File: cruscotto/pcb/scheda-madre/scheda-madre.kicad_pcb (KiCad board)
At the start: 4 copper layers, 178.7 x 74 mm, 148 parts, among them J1 Micro-Fit 2x12 verso auto (D-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, J10 Verso P1 S3: 5V TXD RXD GND, J11 Verso P2 S3: IO19 IO11 IO12 I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, J12 Verso P6 Speak S3, J3 USB-C (solo a banco), J4 Ventola Delta AFB0412VA-00 (D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, J5 NTC display, J6 STEVAL-MKI196V1 (DIL-24), J7 Modulo MicroSD: 3V3 CS MOSI C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, J8 Modulo VAN: 3.3V GND RX TX, J9 Modulo VAN: CANH CANL, K1 G2RL-2 DC5, K2 G2RL-2 DC5, Q1 IPD50N06S4L-12 (da confermare), Q3 ZXMP6A13F (P 60 V), Q4 MMBTA06 (80 V), Q5 MMBT3904, Q6 MMBT3904, Q7 MMBT3904, Q8 MMBT5551, Q9 AO3400A, SW3 RESET, SW4 BOOT, U1 LM74700-Q1, U10 DS3231SN, U2 TPS54360B, U3 LMR36510, U4 ESP32-WROOM-32E-H4, U5 AP2112K-3.3, U6 CH340C, U7 LM2903B, U9 AP2112K-3.3

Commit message: feat(bom): power parts verified (Q1, L1, L2, C3), complete purchase list per supplier
- Verification 28/10/2026 from DigiKey parameters and TI pages: IPD50N06S4L-12 (0.06 W at 2.2 A,
  LM74700 gate 12.1-13 V below VGS 16 V), SRR1260-8R2Y (Isat 5.8 A, peak 2.45 A at 2 A load),
  SRN6045TA-220M (Isat 3.3 A, peak 1.17 A), EEU-FR1H221 (about 1 ms ride-through; 17.5 mm tall:
  mount lying down). Schematic EL-001 rev D values and notes, board values updated; DRC unchanged
  (0 errors, 0 unconnected).
- lista-acquisti-scheda-madre.md: LCSC cart (55 lines, 84.52 USD + 13 USD shipping), Farnell quick
  order (16 lines incl. second STEVAL and Micro-Fit bench plug), DigiKey L1 and fan, second MicroSD
  and VAN modules, PCB after Gerbers.

Co-Authored-By: Claude Opus 5.5 <noreply@anthropic.com>
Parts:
- L1: value 8.2uH Isat>=5A -> SRR1260-8R2Y
- L2: value 22uH Isat>=1.5A -> SRN6045TA-220M
- Q1: value IPD50N06S4L-12 (da confermare) -> IPD50N06S4L-12
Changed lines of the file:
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@@
 			)
 		)
-		(property "Value" "IPD50N06S4L-12 (da confermare)"
+		(property "Value" "IPD50N06S4L-12"
 			(at 0 4.5 0)
 			(layer "F.Fab")
@@
 			)
 		)
-		(property "Value" "22uH Isat>=1.5A"
+		(property "Value" "SRN6045TA-220M"
 			(at 0 4.2 0)
 			(layer "F.Fab")
@@
 			)
 		)
-		(property "Value" "8.2uH Isat>=5A"
+		(property "Value" "SRR1260-8R2Y"
 			(at 0 7.4 0)
 			(layer "F.Fab")

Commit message: feat(pcb): silkscreen for hand assembly, assembly drawings and soldering guide
- tools/serigrafia-scheda-madre.py: reference designators 1.0 mm (0.8 mm where needed) placed clear of
  pads, outlines, edge and holes; pin-1 dots on ICs, transistors, modules and connectors; wire names
  next to the solder pads (J4, J5, J10-J12) and module pins; title and side on F and B.
  DRC: 0 violations including warnings (was 92 silkscreen warnings).
- STEVAL footprint: pin-1 chamfer crossed pad 1, removed (square pad and dot mark pin 1).
- montaggio/: assembly drawings per side (PDF, vector) and assembly list with position and polarity;
  cruscotto/docs/montaggio-scheda-madre.md: order of assembly, polarity conventions, wire colours,
  checks before first power-up (procedure, not executed).

Open: VAN module (J8/J9) has a right-angle header and a screw terminal: mounting to be decided.

Co-Authored-By: Claude Opus 5.5 <noreply@anthropic.com>
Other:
- board text added: "​12V"
- board text added: "​3V3"
- board text added: "​5V"
- board text added: "​C3+AI scheda madre · LATO S3"
- board text added: "​C3+AI scheda madre · RETRO · rev A 10/2026"
- board text added: "​CS"
- board text added: "​GND"
- board text added: "​IO11"
- board text added: "​IO12"
- board text added: "​IO13"
- board text added: "​IO19"
- board text added: "​NTC"
- board text added: "​PWM"
- board text added: "​RPM"
- board text added: "​RX"
- board text added: "​RXD"
- board text added: "​SPK"
- board text added: "​TX"
- board text added: "​TXD"

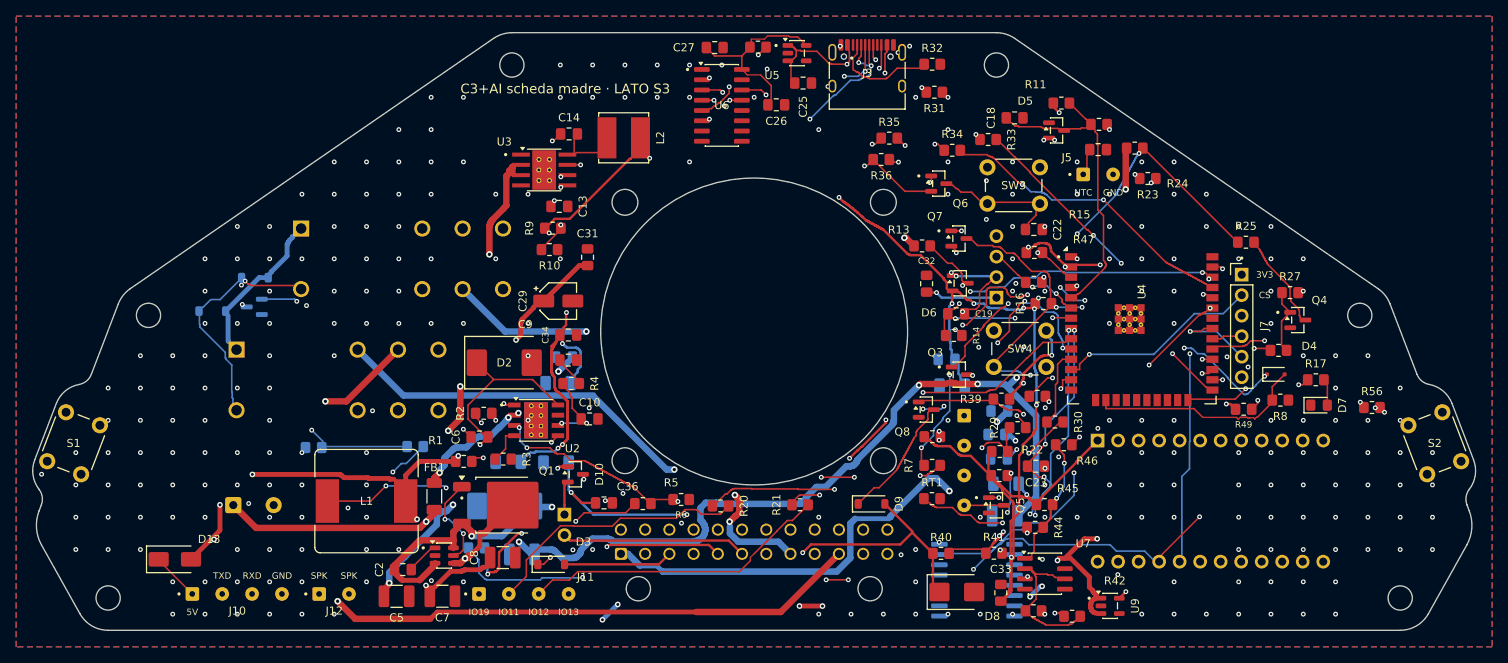
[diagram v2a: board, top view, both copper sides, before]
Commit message: feat(pcb): D-060 VAN module soldered flat on the back, re-routed; 3D envelopes with fan for the STEP
- D-060: VAN module footprint Modulo_VAN_SN65HVD230 (4 straight pins on J8, 35 x 13 mm body on the
  back, over the U4 thermal vias: mount after U4); CANH/CANL by two wires from the module screw
  terminal to J9 pads. J8 and J9 were wrongly placed as two separate connectors 53 mm apart.
  Schematic EL-003 rev C. Generator: body on one side only for J8 and U4 (thermal vias kept free).
- completa-sbroglio: stuck nets may also rip up nearby power tracks (not ground).
- Board: 5653 tracks, 566 vias; DRC 0 violations including warnings, 0 unconnected.
- tools/modelli-3d-scheda-madre.py: STEP envelope boxes for parts without KiCad models (relays,
  C3 17.5 mm, J1, USB-C, U2, STEVAL, VAN module) and the Delta fan 40 x 40 x 10 on the back (VENT1,
  mechanical only). Silkscreen, assembly drawings, assembly list and previews regenerated.

Co-Authored-By: Claude Opus 5.5 <noreply@anthropic.com>
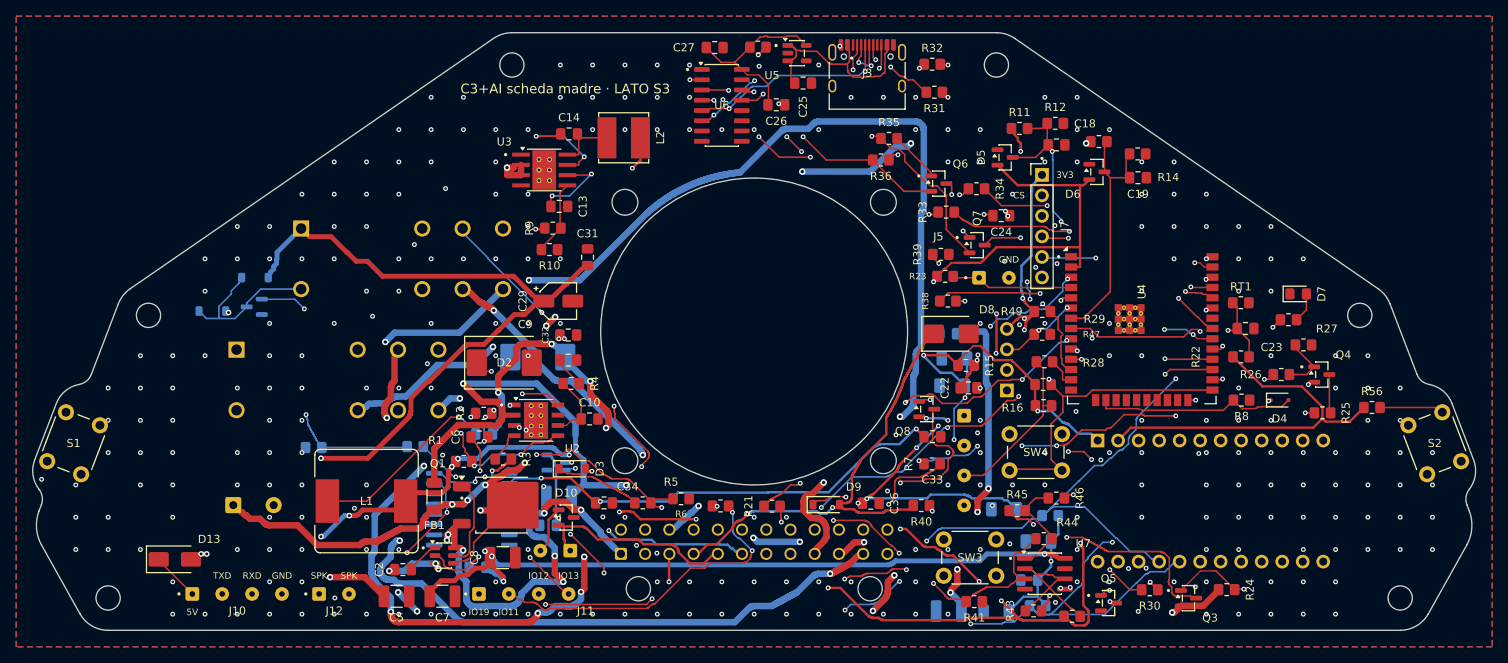
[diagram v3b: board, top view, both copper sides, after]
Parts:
- added VENT1: Delta AFB0412VA-00, , B.Cu at (148.5, 105.0)
- J8: footprint PinHeader_1x04_P2.54mm_Vertical -> Modulo_VAN_SN65HVD230
- J9: footprint PinHeader_1x02_P2.54mm_Vertical -> SolderWire-0.127sqmm_1x02_P3.7mm_D0.48mm_OD1mm
- R19, U9: moved to B.Cu
- moved R18 71.2 mm to (185.2, 127.8)
- moved U9 70.9 mm to (124.0, 121.2), turned to 180 degrees
- moved C15 66.4 mm to (183.7, 131.0)
- moved C28 66.3 mm to (114.2, 134.2)
- moved C1 63.9 mm to (115.1, 117.7)
- moved U10 63.2 mm to (113.5, 127.0)
- moved C17 61.2 mm to (178.5, 139.7)
- moved C30 56.4 mm to (123.0, 129.0)
- moved R24 55.8 mm to (207.0, 137.0)
- moved C35 55.8 mm to (179.4, 127.0)
- moved C12 47.7 mm to (172.5, 105.3)
- moved SW3 46.4 mm to (172.0, 130.8)
- moved RT1 45.3 mm to (208.8, 101.4)
- moved C32 44.8 mm to (125.5, 105.4), turned to 0 degrees
- moved Q3 39.6 mm to (202.3, 138.0)
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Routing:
- net RADIO_L_N: track 67.6 -> 148.2 mm, vias 0 -> 4
- net KEY_IN: track 134.3 -> 191.2 mm, vias 2 -> 12
- net I2C_SCL: track 97.6 -> 153.9 mm, vias 7 -> 6
- net +12V_F: track 221.0 -> 272.6 mm, vias 14 -> 11
- net Net-(Q6-C): track 22.3 -> 72.4 mm, vias 1 -> 7
- net NTC_PCB: track 73.3 -> 29.2 mm, vias 9 -> 2
- net +3V3_SW: track 193.3 -> 155.9 mm, vias 8 -> 10
- net LINK_S32FE: track 38.2 -> 70.1 mm, vias 0 -> 5
- net Net-(J4-Pin_2): track 8.54 -> 37.3 mm
- net FAN_PWM: track 9.63 -> 36.2 mm, vias 0 -> 4
- net RADIO_R_N: track 59.1 -> 82.1 mm, vias 0 -> 5
- net VBAT_P: track 171.0 -> 148.4 mm, vias 3 -> 10
- net I2C_SDA: track 172.4 -> 149.9 mm, vias 8 -> 9
- net Net-(D4-K): track 68.1 -> 46.5 mm, vias 8 -> 6
- net SD_SCK: track 3.76 -> 25.1 mm, vias 0 -> 3
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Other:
- board text added: "​CANH"
- board text added: "​CANL"
- board text removed: "​NTC"
